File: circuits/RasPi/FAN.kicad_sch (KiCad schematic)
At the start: 5 parts, among them J13 Conn_01x03_MountingPin, Q25 BSS138, Q26 SSM3J332R

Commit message: 更新
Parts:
- removed Q25: BSS138, Package_TO_SOT_SMD:SOT-23, symbol Device:Q_NMOS_GSD
- added Q25: 2N7002, Package_TO_SOT_SMD:SOT-23, symbol Transistor_FET:2N7002
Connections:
- net FAN_PWRCtrl: now also Q25.1 (G)
- net GNDD: now also Q25.2 (S)
- net at Q26.1 (G), R102.1: now also Q25.3 (D)
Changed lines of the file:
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@@
   (junction (at 142.24 99.06) (diameter 0) (color 0 0 0 0)
   )
+  (junction (at 134.62 88.9) (diameter 0) (color 0 0 0 0)
+  )
   (junction (at 134.62 71.12) (diameter 0) (color 0 0 0 0)
-  )
-  (junction (at 134.62 88.9) (diameter 0) (color 0 0 0 0)
   )
   (junction (at 142.24 81.28) (diameter 0) (color 0 0 0 0)
@@
     )
   )
+  (symbol (lib_id "Transistor_FET:2N7002") (at 139.7 88.9 0) (unit 1)
+    (in_bom yes) (on_board yes) (dnp no)
+    (property "Reference" "Q25" (at 144.78 91.44 0)
+      (effects (font (size 1.27 1.27)) (justify left))
+    )
+    (property "Value" "2N7002" (at 144.78 93.98 0)
+      (effects (font (size 1.27 1.27)) (justify left))
+    )
+    (property "Footprint" "Package_TO_SOT_SMD:SOT-23" (at 144.78 90.805 0)
+      (effects (font (size 1.27 1.27) italic) (justify left) hide)
+    )
+    (property "Datasheet" "https://www.onsemi.com/pub/Collateral/NDS7002A-D.PDF" (at 144.78 92.71 0)
+      (effects (font (size 1.27 1.27)) (justify left) hide)
+    )
+    (pin "3")
+    (pin "1")
+    (pin "2")
+    (instances
+      (project "RasPi"
+        (path "/689a9e74-f202-4ea4-bfbb-4341f2549250/fddad0c3-2af8-46e3-8794-fa1122d24d51/ffa9c1a5-d3a0-4e0c-a61b-1846c86fcc40"
+          (reference "Q25") (unit 1)
+        )
+      )
+    )
+  )
   (symbol (lib_id "power:GNDD") (at 157.48 78.74 0) (unit 1)
     (in_bom yes) (on_board yes) (dnp no)
@@
         )
       )
-    )
-  )
-  (symbol (lib_name "Q_NMOS_GSD_1") (lib_id "Device:Q_NMOS_GSD") (at 139.7 88.9 0) (unit 1)
-    (in_bom yes) (on_board yes) (dnp no)
-    (property "Reference" "Q25" (at 144.78 91.44 0)
-      (effects (font (size 1.27 1.27)) (justify left))
-    )
-    (property "Value" "BSS138" (at 144.78 93.98 0)
-      (effects (font (size 1.27 1.27)) (justify left))
-    )
-    (property "Footprint" "Package_TO_SOT_SMD:SOT-23" (at 144.78 86.36 0)
-      (effects (font (size 1.27 1.27)) hide)
-    )
-    (property "Datasheet" "~" (at 139.7 88.9 0)
-      (effects (font (size 1.27 1.27)) hide)
-    )
-    (pin "1")
-    (pin "2")
-    (pin "3")
-    (instances
-      (project "RasPi"
-        (path "/689a9e74-f202-4ea4-bfbb-4341f2549250/fddad0c3-2af8-46e3-8794-fa1122d24d51/ffa9c1a5-d3a0-4e0c-a61b-1846c86fcc40"
-          (reference "Q25") (unit 1)
-        )
-      )

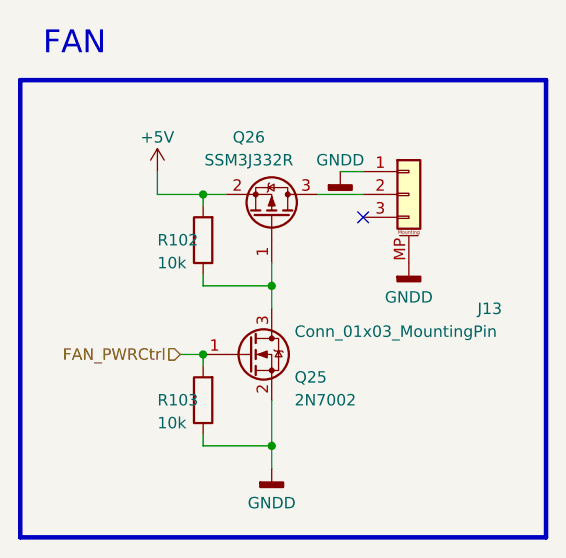
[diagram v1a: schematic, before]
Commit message: 発注第2弾
RasPi発注
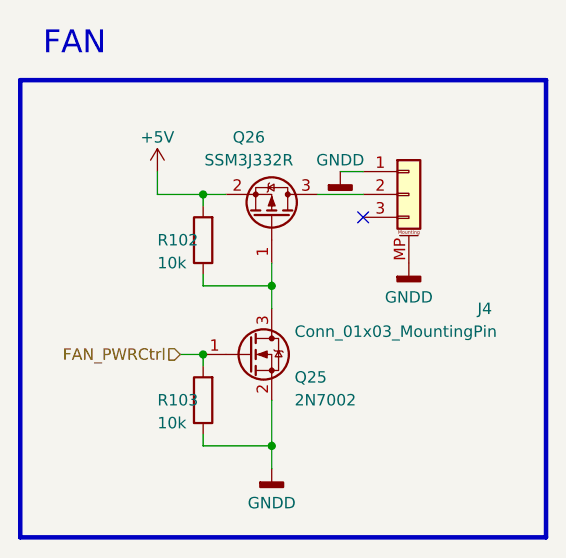
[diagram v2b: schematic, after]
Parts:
- renumbered J13 to J4
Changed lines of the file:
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@@
   (symbol (lib_id "Connector_Generic_MountingPin:Conn_01x03_MountingPin") (at 157.48 71.12 0) (unit 1)
     (in_bom yes) (on_board yes) (dnp no)
-    (property "Reference" "J13" (at 165.1 83.82 0)
+    (property "Reference" "J4" (at 165.1 83.82 0)
       (effects (font (size 1.27 1.27)) (justify left))
     )
@@
       (project "RasPi"
         (path "/689a9e74-f202-4ea4-bfbb-4341f2549250/fddad0c3-2af8-46e3-8794-fa1122d24d51/ffa9c1a5-d3a0-4e0c-a61b-1846c86fcc40"
-          (reference "J13") (unit 1)
+          (reference "J4") (unit 1)
         )
       )
